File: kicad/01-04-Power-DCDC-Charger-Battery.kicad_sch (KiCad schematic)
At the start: 0 parts

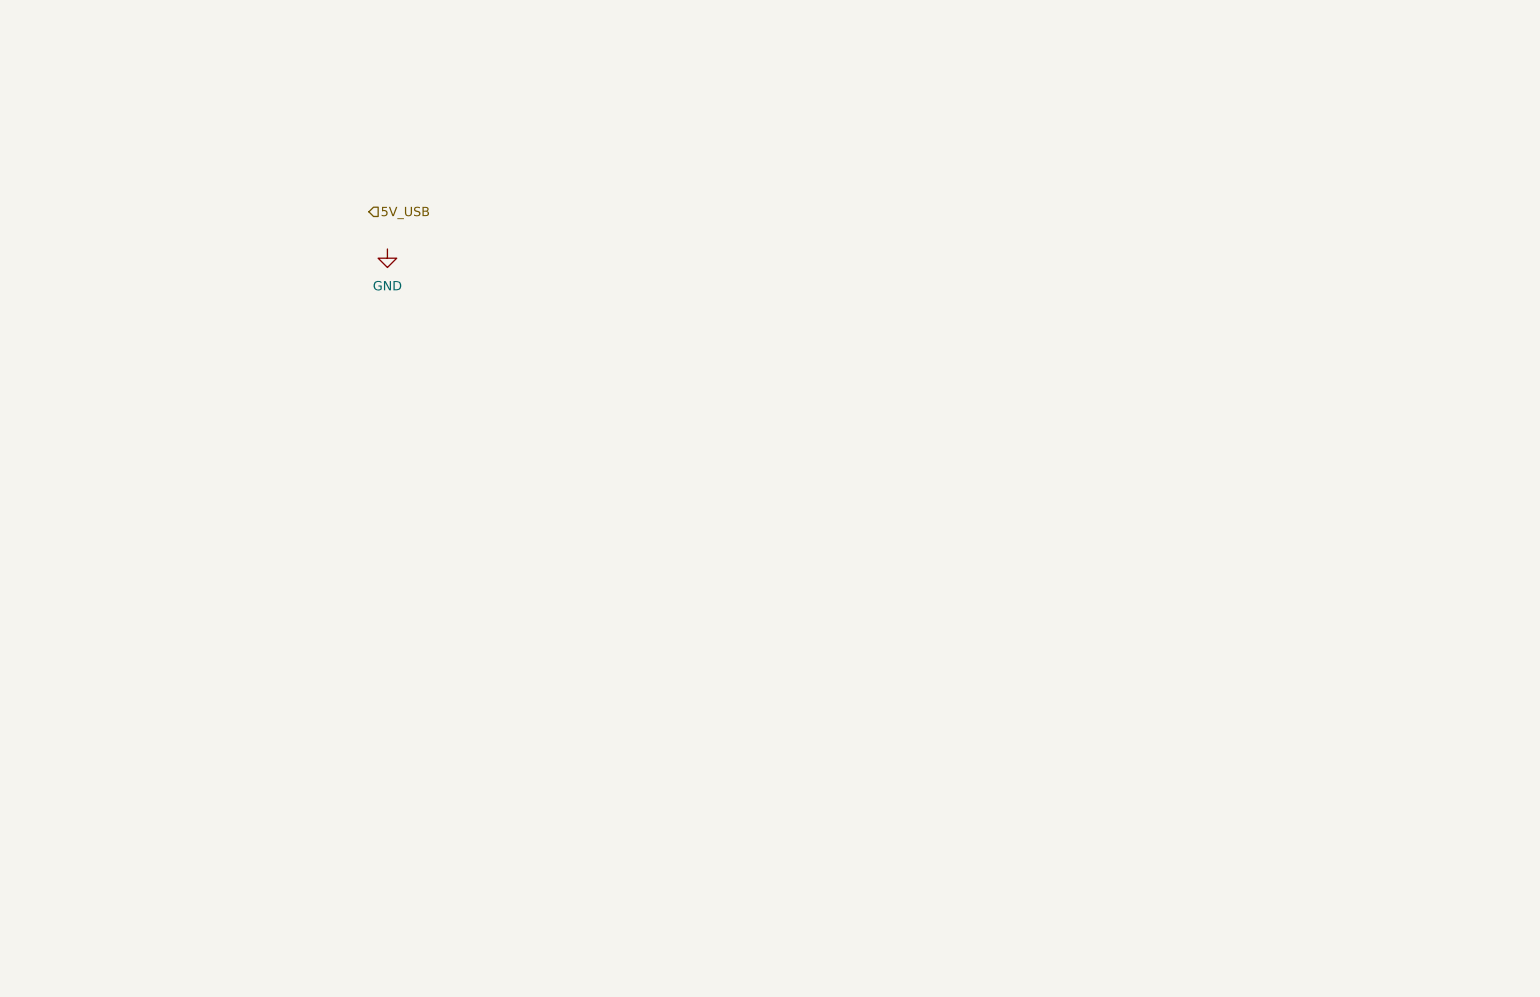
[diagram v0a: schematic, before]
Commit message: added charger and power mux
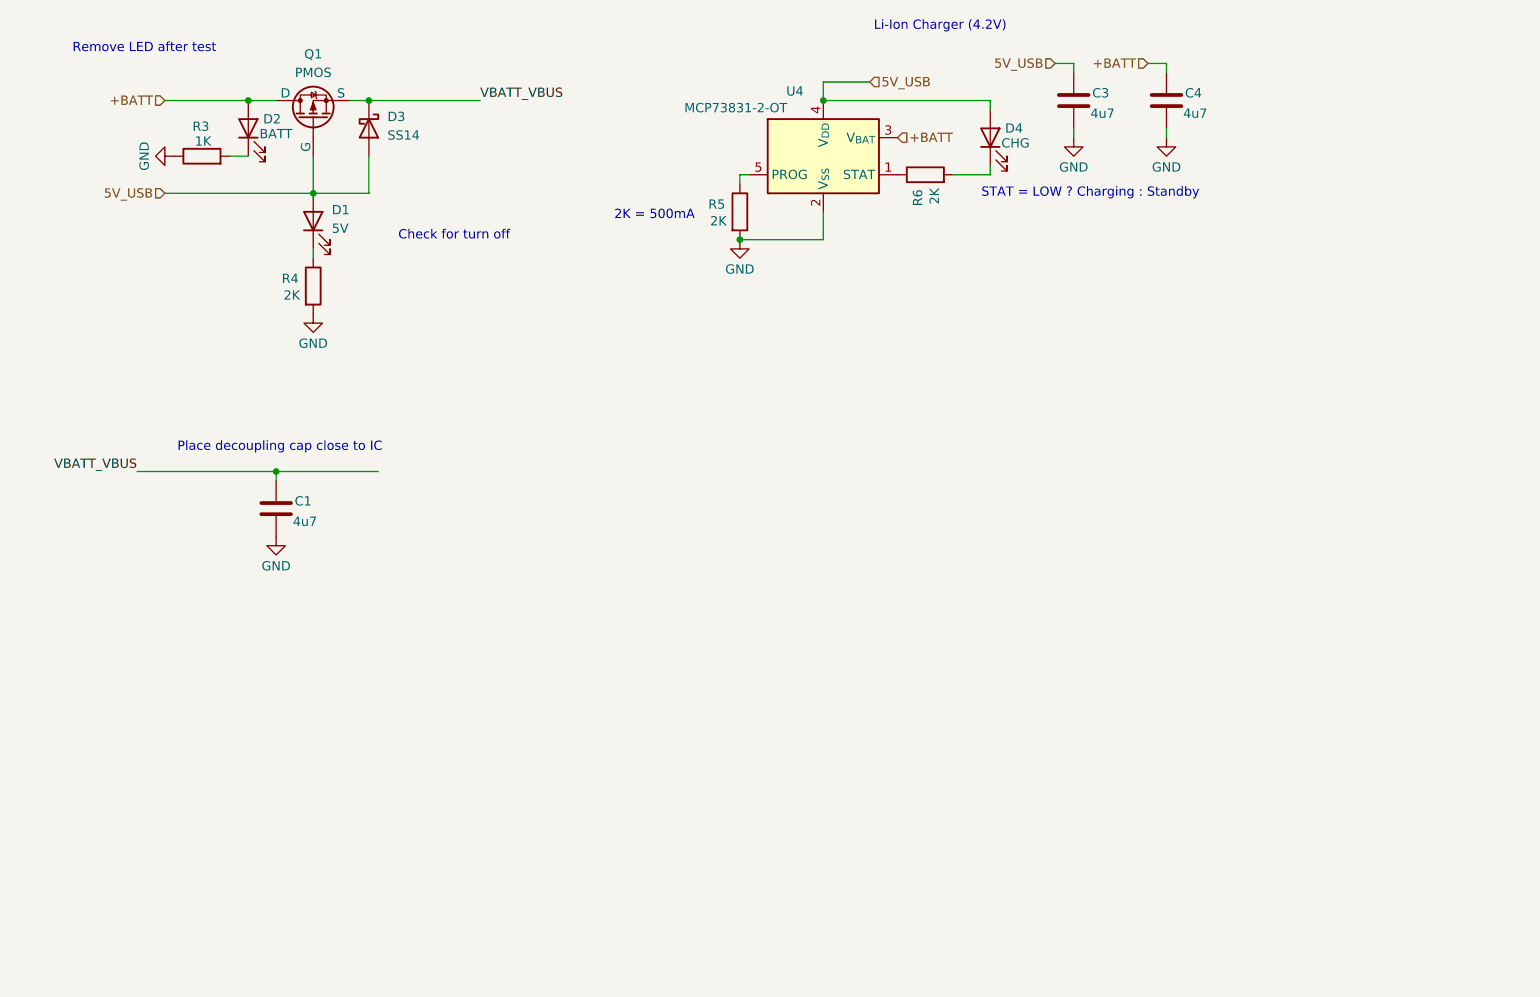
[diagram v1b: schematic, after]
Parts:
- added C1, C3, C4: 4u7, symbol Device:C
- added D1: 5V, LED_SMD:LED_0805_2012Metric, symbol Device:LED
- added D2: BATT, LED_SMD:LED_0805_2012Metric, symbol Device:LED
- added D3: SS14, Diode_SMD:D_SMA, symbol Diode:SS14
- added D4: CHG, LED_SMD:LED_0805_2012Metric, symbol Device:LED
- added Q1: PMOS, Package_TO_SOT_SMD:SOT-23, symbol Simulation_SPICE:PMOS
- added R3: 1K, symbol Device:R
- added R4, R5, R6: 2K, symbol Device:R
- added U4: MCP73831-2-OT, Package_TO_SOT_SMD:SOT-23-5, symbol Battery_Management:MCP73831-2-OT
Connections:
- net 5V_USB: now also C3.1, D1.2 (A), D3.2 (A), D4.2 (A), Q1.2 (G), U4.4 (V_{DD})
- net GND: now also C1.2, C3.2, C4.2, R3.1, R4.2, R5.2, U4.2 (V_{SS})
- new net: R6.1, U4.1 (STAT)
- new net: R5.1, U4.5 (PROG)
- new net: D1.1 (K), R4.1
- new net: D4.1 (K), R6.2
- new net: D2.1 (K), R3.2
- new net +BATT: C4.1, D2.2 (A), Q1.1 (D), U4.3 (V_{BAT})
- new net VBATT_VBUS: C1.1, D3.1 (K), Q1.3 (S)
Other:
- note added: "2K = 500mA"
- note added: "Check for turn off"
- note added: "Li-Ion Charger (4.2V)"
- note added: "Place decoupling cap close to IC"
- note added: "Remove LED after test"
- note added: "STAT = LOW ? Charging : Standby"

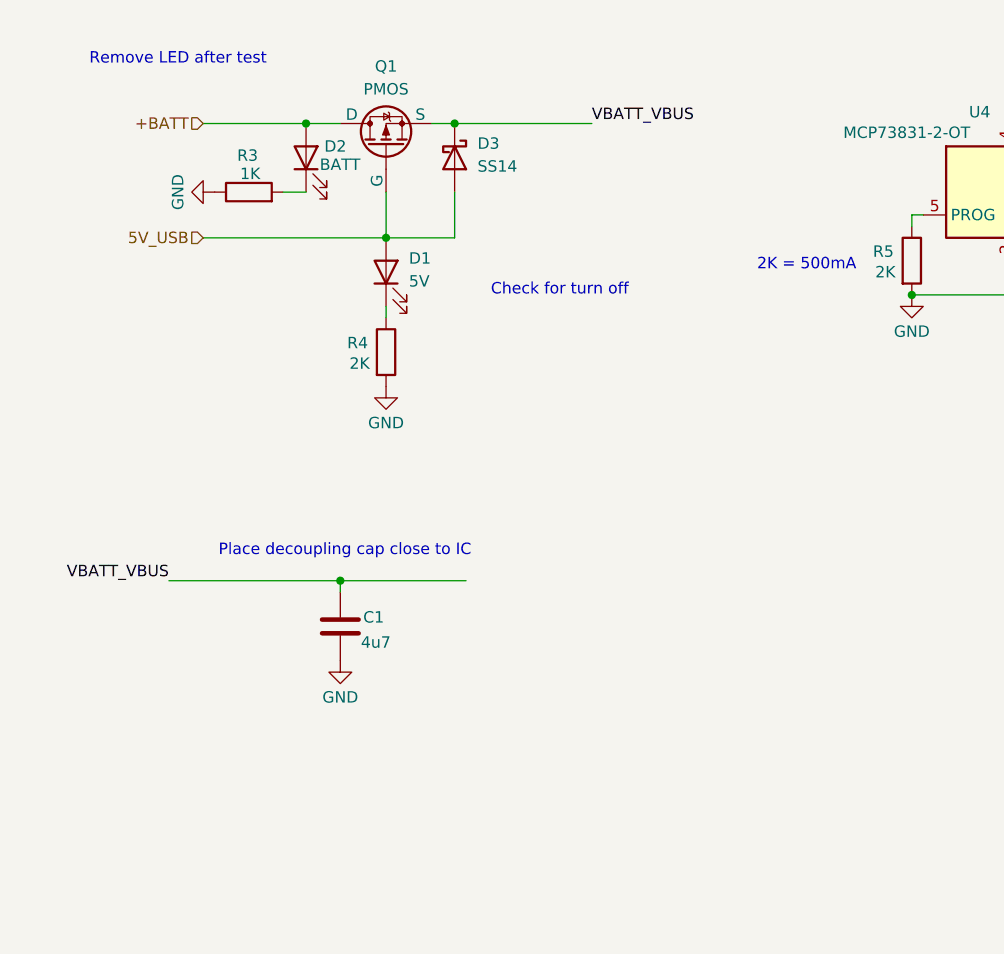
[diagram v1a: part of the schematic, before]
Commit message: battery charger and protection
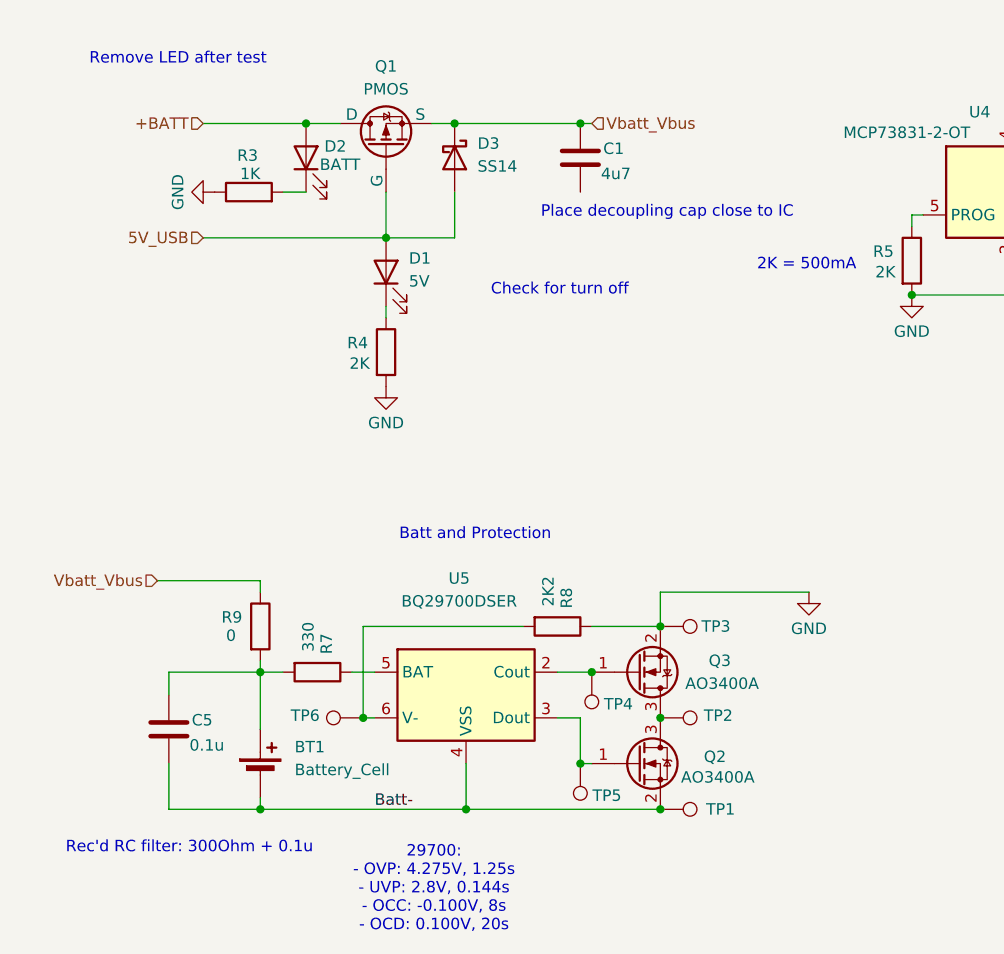
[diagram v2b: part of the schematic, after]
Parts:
- added BT1: Battery_Cell, symbol Device:Battery_Cell
- added C5: 0.1u, symbol Device:C
- added Q2, Q3: AO3400A, Package_TO_SOT_SMD:SOT-23, symbol Transistor_FET:AO3400A
- added R7: 330, symbol Device:R
- added R8: 2K2, symbol Device:R
- added R9: 0, symbol Device:R
- added TP1, TP2, TP3, TP4, TP5, TP6: TestPoint, symbol Connector:TestPoint
- added U5: BQ29700DSER, Package_SON:WSON-6_1.5x1.5mm_P0.5mm, symbol Battery_Management:BQ297xy
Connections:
- net GND: now also Q3.2 (S), R8.1, TP3.1; no longer C1.2
- net VBATT_VBUS renamed Vbatt_Vbus
- net Vbatt_Vbus: now also R9.1
- new net: R8.2, TP6.1, U5.6 (V-)
- new net: Q2.1 (G), TP5.1, U5.3 (Dout)
- new net: BT1.1 (+), C5.1, R7.2, R9.2
- new net: Q3.1 (G), TP4.1, U5.2 (Cout)
- new net: R7.1, U5.5 (BAT)
- new net: Q2.3 (D), Q3.3 (D), TP2.1
- new net Batt-: BT1.2 (-), C5.2, Q2.2 (S), TP1.1, U5.4 (VSS)
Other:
- note added: "29700: - OVP: 4.275V, 1.25s - UVP: 2.8V, 0.144s - OCC: -0.100V, 8s - OCD: 0.100V, 20s"
- note added: "Batt and Protection"
- note added: "Rec'd RC filter: 300Ohm + 0.1u"
- moved on the sheet: C1

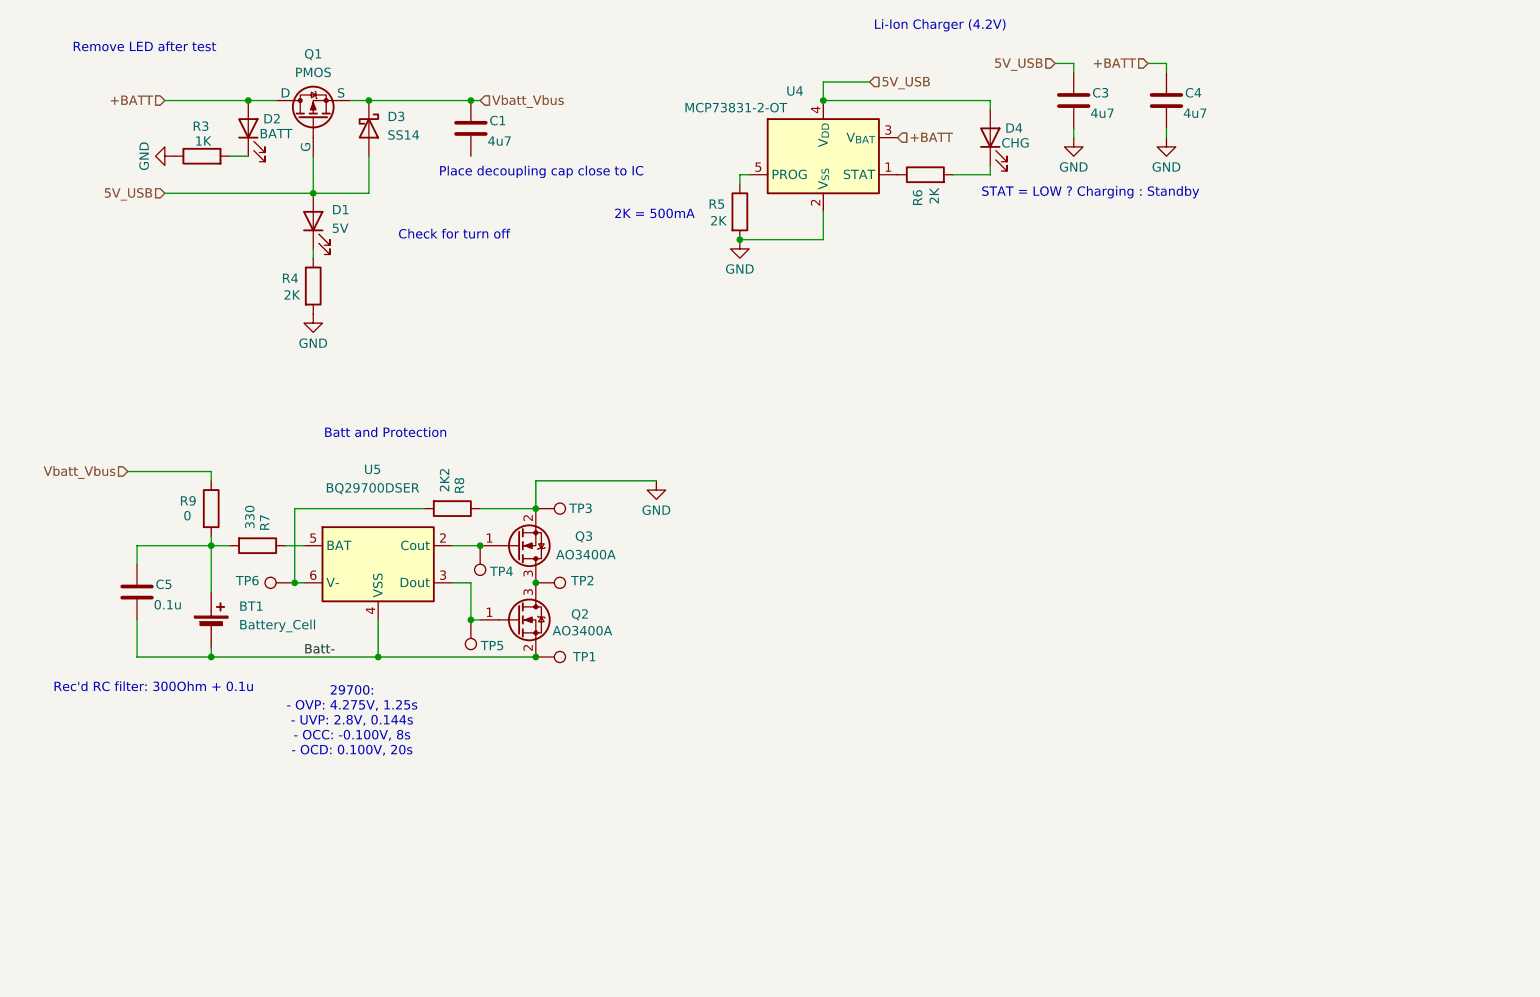
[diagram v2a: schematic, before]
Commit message: battery protection and connector
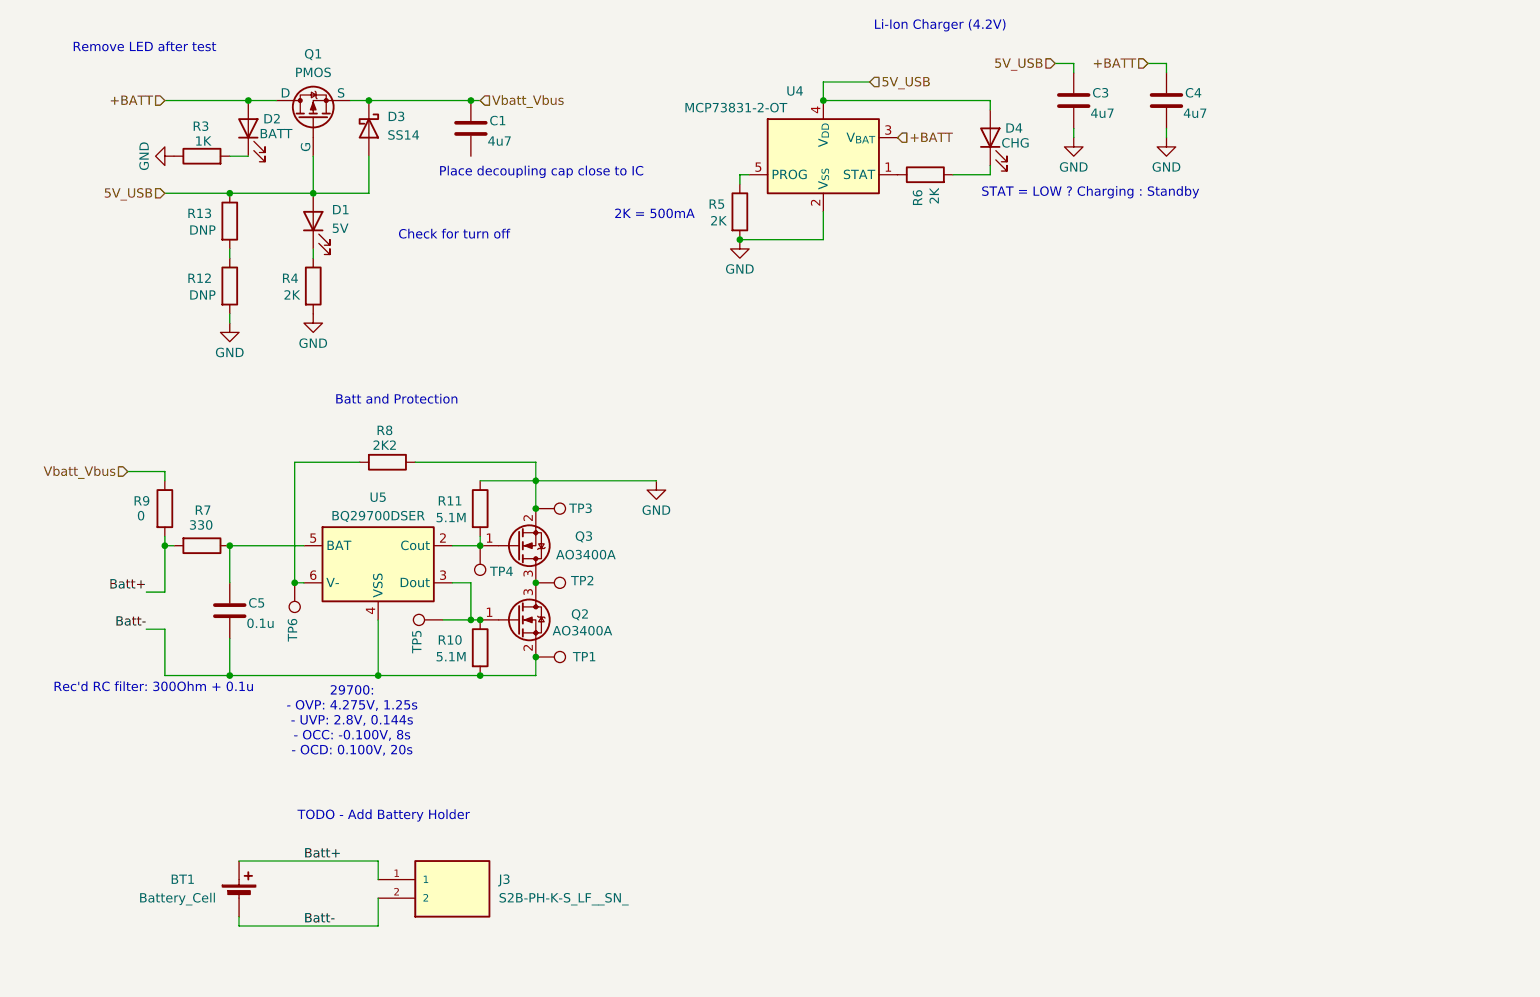
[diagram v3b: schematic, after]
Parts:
- added J3: S2B-PH-K-S_LF__SN_, Connector_JST:JST_PH_S2B-PH-K_1x02_P2.00mm_Horizontal, symbol Project_Library:S2B-PH-K-S_LF__SN_
- added R10, R11: 5.1M, symbol Device:R
- added R12, R13: DNP, symbol Device:R
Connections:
- net 5V_USB: now also R13.1
- net Batt-: now also J3.2, R10.2
- net GND: now also R11.1, R12.2
- net at Q2.1 (G), TP5.1, U5.3 (Dout): now also R10.1
- net Batt+: now reaches BT1.1 (+), R7.2, R9.2
- net Batt+: now also J3.1; no longer C5.1
- net at Q3.1 (G), TP4.1, U5.2 (Cout): now also R11.2
- net at R7.1, U5.5 (BAT): now also C5.1
- new net: R12.1, R13.2
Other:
- note added: "TODO - Add Battery Holder"
- moved on the sheet: BT1, C5, R7, R8, R9, TP5, TP6

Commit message: dc dc start
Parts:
- removed C1: 4u7, symbol Device:C
- added C6: 22u, symbol Device:C
- added C7: 6.8p, Capacitor_SMD:C_0603_1608Metric_Pad1.08x0.95mm_HandSolder, symbol Device:C
- added C8: 4.7u, symbol Device:C
- added L1: 2.2u, project footprints:IND_SDER041H-2R2MS, symbol Device:L
- added R14: 200K, symbol Device:R
- added R15: 44.2K, symbol Device:R
- added U6: TLV62568DBV, Package_TO_SOT_SMD:SOT-23-5, symbol Regulator_Switching:TLV62568DBV
- C3, C4: value 4u7 -> 4.7u
- R8: value 2K2 -> 2.2K
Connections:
- net GND: now also C6.2, C8.2, R15.2, U6.2 (GND)
- net Vbatt_Vbus: no longer R9.1
- net +BATT renamed Vbatt
- net Vbatt: now also R9.1
- new net: C8.1, U6.4 (VIN)
- new net: C7.2, R14.2, R15.1, U6.5 (FB)
- new net: C6.1, C7.1, L1.2, R14.1
- new net: L1.1, U6.3 (SW)
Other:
- note added: "## Batt and Protection"
- note added: "## DCDC"
- note added: "## Li-ion Charger"
- note added: "## Power Mux"
- note added: "R14/R15 for 3.31V out"
- note added: "TODO - power control & GPIO block"
- note removed: "Batt and Protection"
- note removed: "Li-Ion Charger (4.2V)"
- note removed: "Place decoupling cap close to IC"
- note removed: "Rec'd RC filter: 300Ohm + 0.1u"
- moved on the sheet: BT1, C3, C4, C5, D1, D2, D3, D4, J3, Q1, Q2, Q3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
